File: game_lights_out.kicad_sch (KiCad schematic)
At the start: 92 parts, among them SW1 SW_MEC_5E, SW10 SW_MEC_5E, SW11 SW_MEC_5E, SW12 SW_MEC_5E, SW13 SW_MEC_5E, SW14 SW_MEC_5E, SW15 SW_MEC_5E, SW16 SW_MEC_5E, SW17 SW_MEC_5E, SW18 SW_MEC_5E, SW19 SW_MEC_5E, SW2 SW_MEC_5E, SW20 SW_MEC_5E, SW21 SW_MEC_5E, SW22 SW_MEC_5E, SW23 SW_MEC_5E, SW24 SW_MEC_5E, SW25 SW_MEC_5E, SW26 SW_MEC_5E, SW27 SW_MEC_5E, SW28 SW_MEC_5E, SW29 SW_MEC_5E, SW3 SW_MEC_5E, SW30 SW_MEC_5E, SW31 SW_MEC_5E, SW32 SW_MEC_5E, SW33 SW_MEC_5E, SW34 SW_MEC_5E, SW35 SW_MEC_5E, SW36 SW_MEC_5E, SW37 SW_MEC_5E, SW38 SW_MEC_5E, SW39 SW_MEC_5E, SW4 SW_MEC_5E, SW40 SW_MEC_5E, SW5 SW_MEC_5E, SW6 SW_MEC_5E, SW7 SW_MEC_5E, SW8 SW_MEC_5E, SW9 SW_MEC_5E, U1 ATmega328-P, U2 ULN2803A

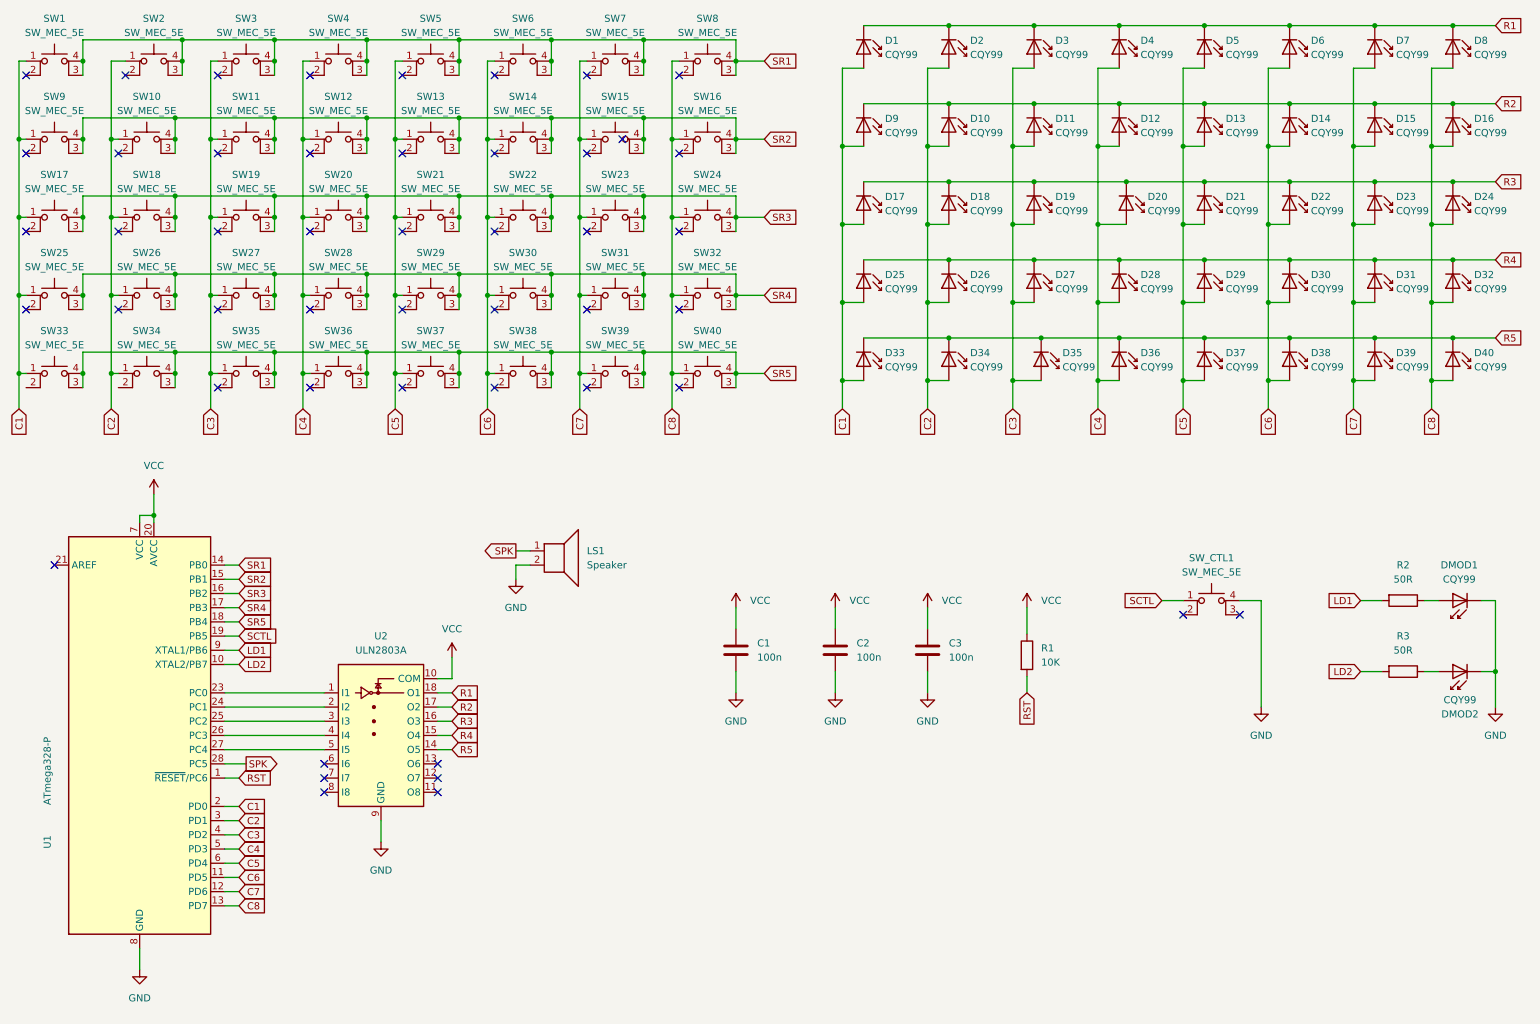
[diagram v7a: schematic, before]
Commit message: Major circuit redesign - matrix size is now 7 x 6 - resistors for matrix LEDs - game mode LEDs driven by single pin (cannot light simultaneously)
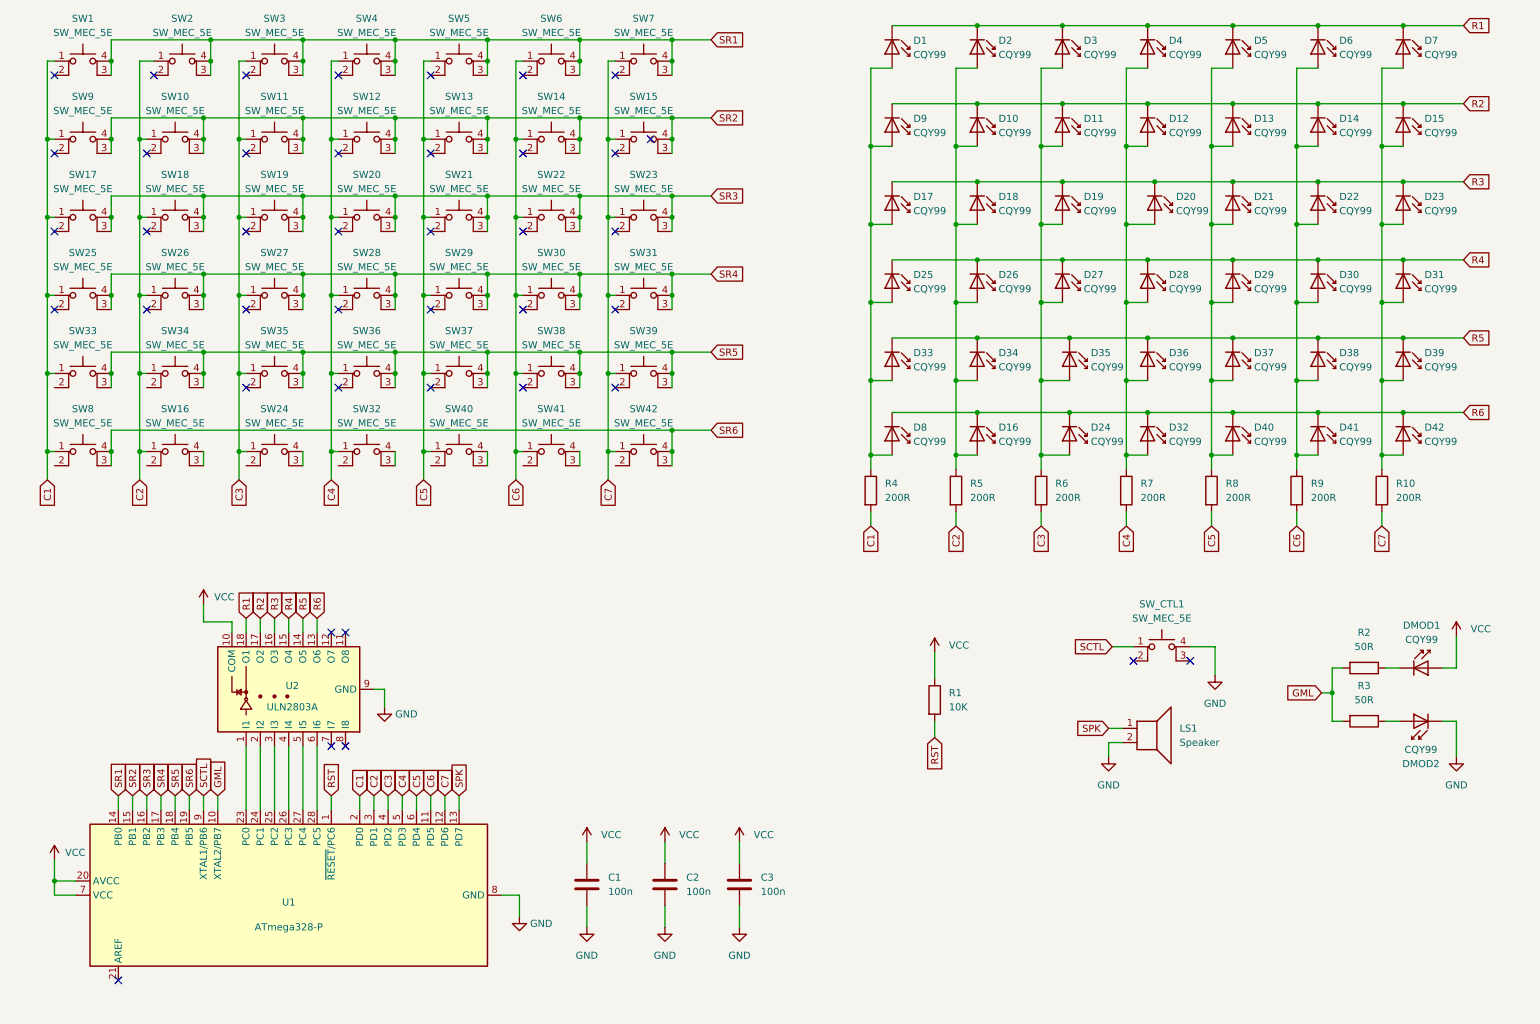
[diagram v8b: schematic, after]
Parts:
- added D41, D42: CQY99, LED_THT:LED_D5.0mm, symbol LED:CQY99
- added R10, R4, R5, R6, R7, R8, R9: 200R, Resistor_THT:R_Axial_DIN0207_L6.3mm_D2.5mm_P7.62mm_Horizontal, symbol Device:R
- added SW41, SW42: SW_MEC_5E, kicad_footprints:SW_PUSH_6mm_H5mm, symbol Switch:SW_MEC_5E
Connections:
- net LD2 is gone; now on net GML: R3.2, U1.10 (XTAL2/PB7)
- net C1: now also SW8.1, R4.2; no longer D1.2 (A), D17.2 (A), D25.2 (A), D33.2 (A), D9.2 (A)
- net C2: now also SW16.1, R5.2; no longer D10.2 (A), D18.2 (A), D2.2 (A), D26.2 (A), D34.2 (A)
- net C3: now also SW24.1, R6.2; no longer D11.2 (A), D19.2 (A), D27.2 (A), D3.2 (A), D35.2 (A)
- net C4: now also SW32.1, R7.2; no longer D12.2 (A), D20.2 (A), D28.2 (A), D36.2 (A), D4.2 (A)
- net C5: now also SW40.1, R8.2; no longer D13.2 (A), D21.2 (A), D29.2 (A), D37.2 (A), D5.2 (A)
- net C6: now also R9.2, SW41.1; no longer D14.2 (A), D22.2 (A), D30.2 (A), D38.2 (A), D6.2 (A)
- net C7: now also R10.2, SW42.1; no longer D15.2 (A), D23.2 (A), D31.2 (A), D39.2 (A), D7.2 (A)
- net GND: no longer DMOD1.1 (K)
- net R1: no longer D8.1 (K)
- net R2: no longer D16.1 (K)
- net R3: no longer D24.1 (K)
- net R4: no longer D32.1 (K)
- net R5: no longer D40.1 (K)
- net SCTL: now also U1.9 (XTAL1/PB6); no longer U1.19 (PB5)
- net SPK: now also U1.13 (PD7); no longer U1.28 (PC5)
- net SR1: no longer SW8.3 (K), SW8.4 (A)
- net SR2: no longer SW16.3 (K), SW16.4 (A)
- net SR3: no longer SW24.3 (K), SW24.4 (A)
- net SR4: no longer SW32.3 (K), SW32.4 (A)
- net SR5: no longer SW40.3 (K), SW40.4 (A)
- net VCC: now also DMOD1.2 (A)
- net at R2.1: now also DMOD1.1 (K); no longer DMOD1.2 (A)
- net R6: now reaches U2.13 (O6)
- net R6: now also D16.1 (K), D24.1 (K), D32.1 (K), D40.1 (K), D8.1 (K), D41.1 (K), D42.1 (K)
- net at U2.6 (I6): now also U1.28 (PC5)
- removed net C8: D16.2 (A), D24.2 (A), D32.2 (A), D40.2 (A), D8.2 (A), SW16.1, SW24.1, SW32.1, SW40.1, SW8.1, U1.13 (PD7)
- net LD1 renamed GML
- net GML: no longer U1.9 (XTAL1/PB6)
- new net: D14.2 (A), D22.2 (A), D30.2 (A), D38.2 (A), D41.2 (A), D6.2 (A), R9.1
- new net: D1.2 (A), D17.2 (A), D25.2 (A), D33.2 (A), D8.2 (A), D9.2 (A), R4.1
- new net: D12.2 (A), D20.2 (A), D28.2 (A), D32.2 (A), D36.2 (A), D4.2 (A), R7.1
- new net: D15.2 (A), D23.2 (A), D31.2 (A), D39.2 (A), D42.2 (A), D7.2 (A), R10.1
- new net: D13.2 (A), D21.2 (A), D29.2 (A), D37.2 (A), D40.2 (A), D5.2 (A), R8.1
- new net: D11.2 (A), D19.2 (A), D24.2 (A), D27.2 (A), D3.2 (A), D35.2 (A), R6.1
- new net: D10.2 (A), D16.2 (A), D18.2 (A), D2.2 (A), D26.2 (A), D34.2 (A), R5.1
- new net: SW24.3 (K), SW24.4 (A)
- new net: SW16.3 (K), SW16.4 (A)
- new net: SW41.3 (K), SW41.4 (A)
- new net: SW40.3 (K), SW40.4 (A)
- new net: SW32.3 (K), SW32.4 (A)
- new net SR6: SW42.3 (K), SW42.4 (A), SW8.3 (K), SW8.4 (A), U1.19 (PB5)
- no-connect marks 48 -> 41
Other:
- moved on the sheet: C1, C2, C3, D1, D10, D11, D12, D13, D14, D15, D17, D18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
